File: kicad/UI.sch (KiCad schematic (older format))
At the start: 13 parts, among them Q3 NX3020NAKW, SW2 SW_Push

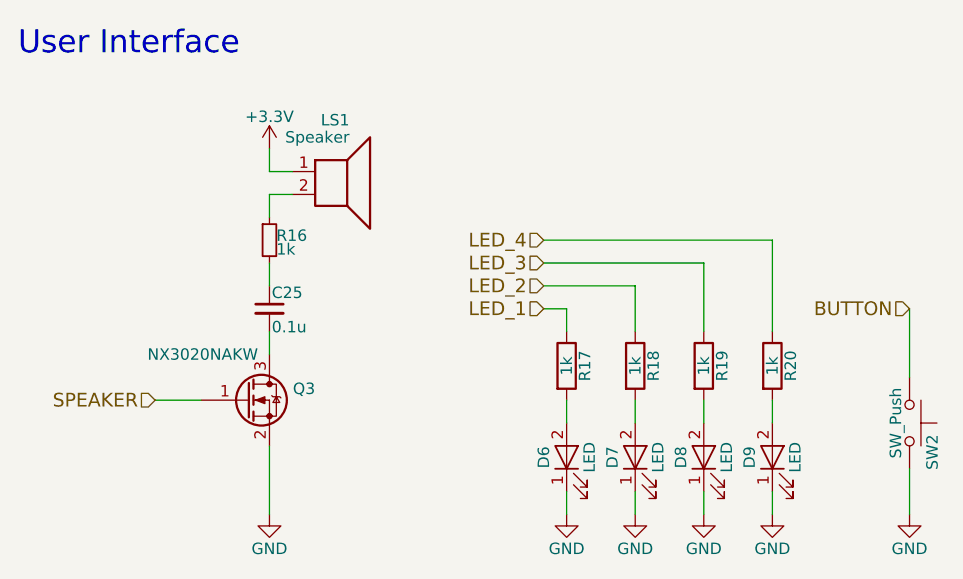
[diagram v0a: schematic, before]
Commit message: 回路とフットプリントを改良
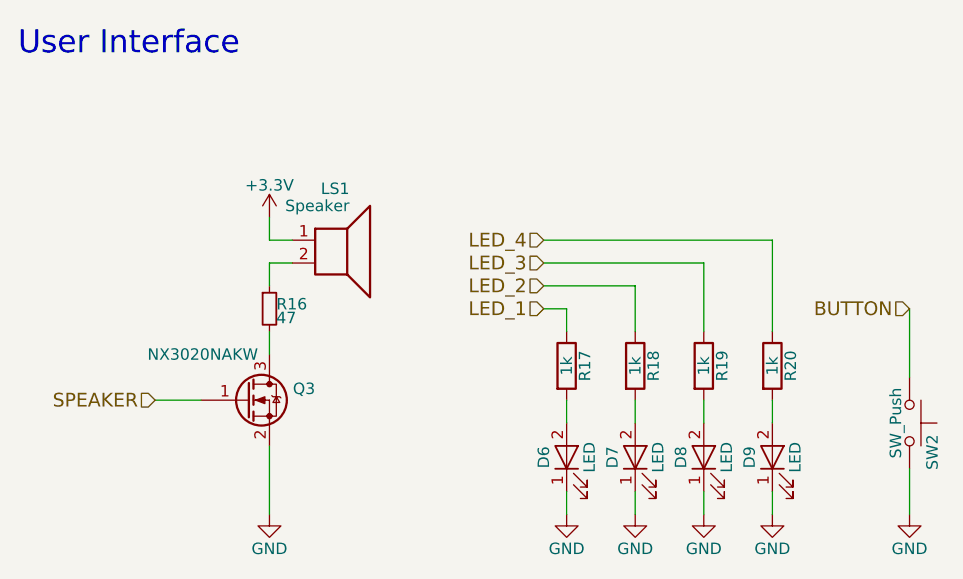
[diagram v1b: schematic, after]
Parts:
- removed C25: 0.1u, Capacitors_SMD:C_0201, symbol C_Small
- R16: value 1k -> 47
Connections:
- net at Q3.3 (D): now also R16.2
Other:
- moved on the sheet: LS1, R16
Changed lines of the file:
@@
 $EndComp
 $Comp
-L GND #PWR046
+L GND #PWR051
 U 1 1 57CE7673
 P 4400 4700
-F 0 "#PWR046" H 4400 4450 50  0001 C CNN
+F 0 "#PWR051" H 4400 4450 50  0001 C CNN
 F 1 "GND" H 4400 4550 50  0000 C CNN
 F 2 "" H 4400 4700 50  0000 C CNN
@@
 SPEAKER
 Wire Wire Line
-	4400 3100 4400 3200
-Wire Wire Line
-	4400 3200 4500 3200
-Wire Wire Line
-	4500 3300 4400 3300
+	4400 3400 4400 3500
+Wire Wire Line
+	4400 3500 4500 3500
+Wire Wire Line
+	4500 3600 4400 3600
 Wire Wire Line
 	4400 4400 4400 4700
@@
 	3900 4200 4100 4200
 $Comp
-L GND #PWR047
+L GND #PWR052
 U 1 1 57CE8530
 P 5700 4700
-F 0 "#PWR047" H 5700 4450 50  0001 C CNN
+F 0 "#PWR052" H 5700 4450 50  0001 C CNN
 F 1 "GND" H 5700 4550 50  0000 C CNN
 F 2 "" H 5700 4700 50  0000 C CNN
@@
 $EndComp
 $Comp
-L GND #PWR048
+L GND #PWR053
 U 1 1 57CE8557
 P 6000 4700
-F 0 "#PWR048" H 6000 4450 50  0001 C CNN
+F 0 "#PWR053" H 6000 4450 50  0001 C CNN
 F 1 "GND" H 6000 4550 50  0000 C CNN
 F 2 "" H 6000 4700 50  0000 C CNN
@@
 	6000 3700 6000 3900
 $Comp
-L GND #PWR049
+L GND #PWR054
 U 1 1 57CEA2EF
 P 7200 4700
-F 0 "#PWR049" H 7200 4450 50  0001 C CNN
+F 0 "#PWR054" H 7200 4450 50  0001 C CNN
 F 1 "GND" H 7200 4550 50  0000 C CNN
 F 2 "" H 7200 4700 50  0000 C CNN
@@
 User Interface
 $Comp
-L +3.3V #PWR050
+L +3.3V #PWR055
 U 1 1 589CB988
-P 4400 3100
-F 0 "#PWR050" H 4400 2950 50  0001 C CNN
-F 1 "+3.3V" H 4400 3240 50  0000 C CNN
-F 2 "" H 4400 3100 50  0000 C CNN
-F 3 "" H 4400 3100 50  0000 C CNN
-	1    4400 3100
-	1    0    0    -1
-$EndComp
-$Comp
-L GND #PWR051
+P 4400 3400
+F 0 "#PWR055" H 4400 3250 50  0001 C CNN
+F 1 "+3.3V" H 4400 3540 50  0000 C CNN
+F 2 "" H 4400 3400 50  0000 C CNN
+F 3 "" H 4400 3400 50  0000 C CNN
+	1    4400 3400
+	1    0    0    -1
+$EndComp
+$Comp
+L GND #PWR056
 U 1 1 592C69B9
 P 6300 4700
-F 0 "#PWR051" H 6300 4450 50  0001 C CNN
+F 0 "#PWR056" H 6300 4450 50  0001 C CNN
 F 1 "GND" H 6300 4550 50  0000 C CNN
 F 2 "" H 6300 4700 50  0000 C CNN
@@
 Wire Wire Line
 	5600 3600 6300 3600
-$Comp
-L C_Small C25
-U 1 1 594481A2
+Wire Wire Line
+	4400 3600 4400 3700
+Wire Wire Line
+	4400 3900 4400 4000
+$Comp
+L R_Small R16
+U 1 1 5945E920
 P 4400 3800
-F 0 "C25" H 4410 3870 50  0000 L CNN
-F 1 "0.1u" H 4410 3720 50  0000 L CNN
-F 2 "Capacitors_SMD:C_0201" H 4400 3800 50  0001 C CNN
+F 0 "R16" H 4430 3820 50  0000 L CNN
+F 1 "47" H 4430 3760 50  0000 L CNN
+F 2 "Resistors_SMD:R_0201" H 4400 3800 50  0001 C CNN
 F 3 "" H 4400 3800 50  0001 C CNN
 	1    4400 3800
 	1    0    0    -1
 $EndComp
-Wire Wire Line
-	4400 3300 4400 3400
-Wire Wire Line
-	4400 3600 4400 3700
-$Comp
-L R_Small R16
-U 1 1 5945E920
-P 4400 3500
-F 0 "R16" H 4430 3520 50  0000 L CNN
-F 1 "1k" H 4430 3460 50  0000 L CNN
-F 2 "Resistors_SMD:R_0201" H 4400 3500 50  0001 C CNN
-F 3 "" H 4400 3500 50  0001 C CNN
-	1    4400 3500
-	1    0    0    -1
-$EndComp
-Wire Wire Line
-	4400 4000 4400 3900
 $Comp
 L LED D8
@@
 L Speaker LS1
 U 1 1 594AA6DF
-P 4700 3200
-F 0 "LS1" H 4750 3425 50  0000 R CNN
-F 1 "Speaker" H 4750 3350 50  0000 R CNN
-F 2 "mouse:SMT-0440-S-R" H 4700 3000 50  0001 C CNN
-F 3 "" H 4690 3150 50  0001 C CNN
-	1    4700 3200
+P 4700 3500
+F 0 "LS1" H 4750 3725 50  0000 R CNN
+F 1 "Speaker" H 4750 3650 50  0000 R CNN
+F 2 "mouse:SMT-0440-S-R" H 4700 3300 50  0001 C CNN
+F 3 "" H 4690 3450 50  0001 C CNN
+	1    4700 3500
 	1    0    0    -1
 $EndComp
@@
 	7200 3800 7200 4100
 $Comp
-L GND #PWR052
+L GND #PWR057
 U 1 1 5980F69C
 P 6600 4700
-F 0 "#PWR052" H 6600 4450 50  0001 C CNN
+F 0 "#PWR057" H 6600 4450 50  0001 C CNN
 F 1 "GND" H 6600 4550 50  0000 C CNN
 F 2 "" H 6600 4700 50  0000 C CNN

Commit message: 自動配線1残し
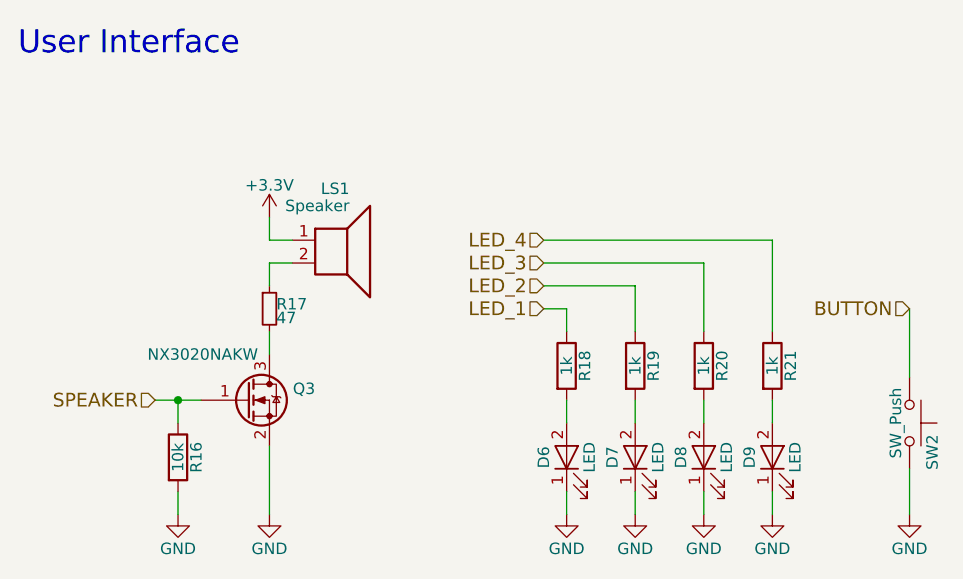
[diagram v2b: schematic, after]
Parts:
- added R16: 10k, Resistors_SMD:R_0201, symbol R
- renumbered R16 to R17, R17 to R18, R18 to R19, R19 to R20, R20 to R21
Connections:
- net GND: now also R16.2
- net SPEAKER: now also R16.1
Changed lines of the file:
@@
 	5700 4600 5700 4700
 $Comp
-L R R17
+L R R18
 U 1 1 57CE8600
 P 5700 4050
-F 0 "R17" V 5780 4050 50  0000 C CNN
+F 0 "R18" V 5780 4050 50  0000 C CNN
 F 1 "1k" V 5700 4050 50  0000 C CNN
 F 2 "Resistors_SMD:R_0201" V 5630 4050 50  0001 C CNN
@@
 $EndComp
 $Comp
-L R R18
+L R R19
 U 1 1 57CE8644
 P 6000 4050
-F 0 "R18" V 6080 4050 50  0000 C CNN
+F 0 "R19" V 6080 4050 50  0000 C CNN
 F 1 "1k" V 6000 4050 50  0000 C CNN
 F 2 "Resistors_SMD:R_0201" V 5930 4050 50  0001 C CNN
@@
 	6300 4700 6300 4600
 $Comp
-L R R19
+L R R20
 U 1 1 592C69C0
 P 6300 4050
-F 0 "R19" V 6380 4050 50  0000 C CNN
+F 0 "R20" V 6380 4050 50  0000 C CNN
 F 1 "1k" V 6300 4050 50  0000 C CNN
 F 2 "Resistors_SMD:R_0201" V 6230 4050 50  0001 C CNN
@@
 	4400 3900 4400 4000
 $Comp
-L R_Small R16
+L R_Small R17
 U 1 1 5945E920
 P 4400 3800
-F 0 "R16" H 4430 3820 50  0000 L CNN
+F 0 "R17" H 4430 3820 50  0000 L CNN
 F 1 "47" H 4430 3760 50  0000 L CNN
 F 2 "Resistors_SMD:R_0201" H 4400 3800 50  0001 C CNN
@@
 	6600 4700 6600 4600
 $Comp
-L R R20
+L R R21
 U 1 1 5980F6A3
 P 6600 4050
-F 0 "R20" V 6680 4050 50  0000 C CNN
+F 0 "R21" V 6680 4050 50  0000 C CNN
 F 1 "1k" V 6600 4050 50  0000 C CNN
 F 2 "Resistors_SMD:R_0201" V 6530 4050 50  0001 C CNN
@@
 Wire Wire Line
 	5600 3500 6600 3500
+$Comp
+L R R16
+U 1 1 59E4BA0F
+P 4000 4450
+F 0 "R16" V 4080 4450 50  0000 C CNN
+F 1 "10k" V 4000 4450 50  0000 C CNN
+F 2 "Resistors_SMD:R_0201" V 3930 4450 50  0001 C CNN
+F 3 "" H 4000 4450 50  0001 C CNN
+	1    4000 4450
+	1    0    0    -1
+$EndComp
+Wire Wire Line
+	4000 4300 4000 4200
+Connection ~ 4000 4200
+$Comp
+L GND #PWR058
+U 1 1 59E4BAB5
+P 4000 4700
+F 0 "#PWR058" H 4000 4450 50  0001 C CNN
+F 1 "GND" H 4000 4550 50  0000 C CNN
+F 2 "" H 4000 4700 50  0000 C CNN
+F 3 "" H 4000 4700 50  0000 C CNN
+	1    4000 4700
+	1    0    0    -1
+$EndComp
+Wire Wire Line
+	4000 4700 4000 4600
 $EndSCHEMATC
